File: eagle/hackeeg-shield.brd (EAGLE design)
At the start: 101.6 x 53.3 mm, 145 parts, among them IC1 ADS1299IPAG, IC10 TXB0108PWR, IC11 TXB0108PWR, IC2 TPS72325DBVT, IC3 TPS73225DBVT, IC5 24AA256UID, IC6 TPS60403DBVT, IC7 OPA376DBV, IC8 OPA376DBV, IC9 TXS0102DCUR

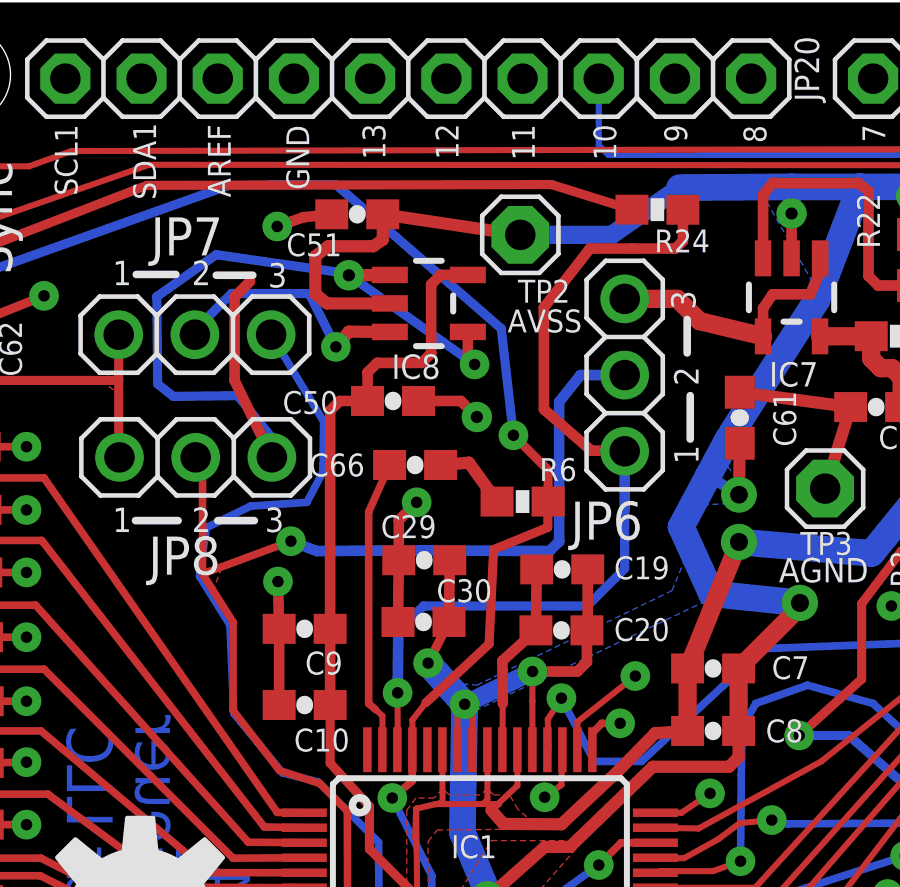
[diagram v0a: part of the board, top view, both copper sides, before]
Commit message: fixed problem with BIASOUT/BIASINV
- for common mode noise rejection
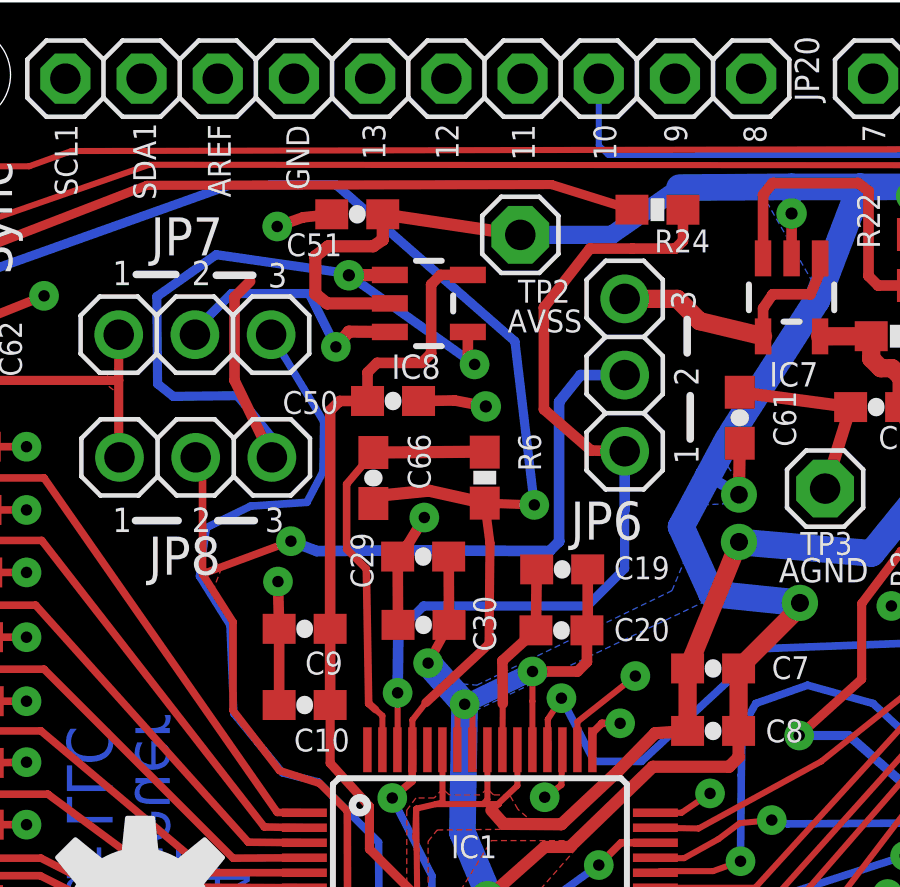
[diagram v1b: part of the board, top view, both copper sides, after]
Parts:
- moved R6 1.49 mm to (32.8, 37.5), turned to 90 degrees
- moved C66 1.46 mm to (29.1, 37.5), turned to 270 degrees
- moved C29 0.13 mm to (30.7, 34.9)
- moved C30 0.10 mm to (30.7, 32.6)
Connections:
- removed net N$22: C66.2, R6.1
- removed net N$25: C66.1, IC1.63
- new net BIASOUT: C66.1, IC1.63, R6.2
- net BIASINV: now also C66.2, R6.1; no longer R6.2
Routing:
- net BIASOUT: track 0.00 -> 14.4 mm
- net N$25: track 9.85 -> 0.00 mm
- net BIASINV: track 85.8 -> 89.9 mm
- net N$22: track 2.55 -> 0.00 mm
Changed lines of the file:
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@@
 <attribute name="VALUE" x="31.3436" y="21.3106" size="0.6096" layer="27"/>
 </element>
-<element name="C29" library="SparkFun-Passives" package="0603-CAP" value="1uF" x="30.7594" y="34.7472" smashed="yes">
-<attribute name="NAME" x="29.3116" y="35.4838" size="0.762" layer="25" font="vector" ratio="12"/>
-<attribute name="VALUE" x="29.7434" y="33.6042" size="0.4064" layer="27" font="vector"/>
-</element>
-<element name="C30" library="SparkFun-Passives" package="0603-CAP" value="1uF" x="30.734" y="32.6898" smashed="yes">
-<attribute name="NAME" x="31.1658" y="33.3502" size="0.762" layer="25" font="vector" ratio="12"/>
-<attribute name="VALUE" x="29.718" y="31.5468" size="0.4064" layer="27" font="vector"/>
+<element name="C29" library="SparkFun-Passives" package="0603-CAP" value="1uF" x="30.72256875" y="34.869375" smashed="yes">
+<attribute name="NAME" x="29.063946875" y="33.812734375" size="0.762" layer="25" font="vector" ratio="12" rot="R90"/>
+<attribute name="VALUE" x="29.70656875" y="33.726375" size="0.4064" layer="27" font="vector"/>
+</element>
+<element name="C30" library="SparkFun-Passives" package="0603-CAP" value="1uF" x="30.734" y="32.592009375" smashed="yes">
+<attribute name="NAME" x="33.151825" y="31.70529375" size="0.762" layer="25" font="vector" ratio="12" rot="R90"/>
+<attribute name="VALUE" x="29.718" y="31.449009375" size="0.4064" layer="27" font="vector"/>
 </element>
 <element name="C31" library="SparkFun-Passives" package="0603-CAP" value="0.01uF" x="82.677" y="47.244" smashed="yes">
@@
 <attribute name="VALUE" x="56.515" y="39.8272" size="0.4064" layer="27" font="vector" rot="R270"/>
 </element>
-<element name="C66" library="SparkFun-Passives" package="0603-CAP" value="0.01uF" x="30.4546" y="37.9222" smashed="yes">
-<attribute name="NAME" x="26.924" y="37.5412" size="0.762" layer="25" font="vector" ratio="12"/>
-<attribute name="VALUE" x="29.4386" y="36.7792" size="0.4064" layer="27" font="vector"/>
-</element>
-<element name="R6" library="SparkFun-Passives" package="0603-RES" value="3.98K" x="34.036" y="36.703" smashed="yes">
-<attribute name="NAME" x="34.5948" y="37.3888" size="0.762" layer="25" font="vector" ratio="12"/>
-<attribute name="VALUE" x="33.02" y="35.56" size="0.4064" layer="27" font="vector"/>
+<element name="C66" library="SparkFun-Passives" package="0603-CAP" value="0.01uF" x="29.062425" y="37.48760625" smashed="yes" rot="R270">
+<attribute name="NAME" x="30.210503125" y="38.961315625" size="0.762" layer="25" font="vector" ratio="12" rot="R270"/>
+<attribute name="VALUE" x="27.919425" y="38.50360625" size="0.4064" layer="27" font="vector" rot="R270"/>
+</element>
+<element name="R6" library="SparkFun-Passives" package="0603-RES" value="3.98K" x="32.774890625" y="37.500809375" smashed="yes" rot="R90">
+<attribute name="NAME" x="34.65220625" y="37.71798125" size="0.762" layer="25" font="vector" ratio="12" rot="R90"/>
+<attribute name="VALUE" x="33.917890625" y="36.484809375" size="0.4064" layer="27" font="vector" rot="R90"/>
 </element>
 <element name="C68" library="SparkFun-Passives" package="0603-CAP" value="1uF" x="51.2572" y="39.116" smashed="yes" rot="R180">
@@
 <wire x1="54.1884" y1="46.0629" x2="54.5567" y2="46.3042" width="0.4064" layer="1"/>
 <wire x1="54.5567" y1="46.3042" x2="56.0714" y2="46.3042" width="0.4064" layer="1"/>
-<wire x1="29.9094" y1="34.7472" x2="29.884" y2="32.6898" width="0.3556" layer="1"/>
+<wire x1="29.87256875" y1="34.869375" x2="29.884" y2="32.592009375" width="0.3556" layer="1"/>
 <wire x1="48.9998" y1="26.935" x2="49.265" y2="26.935" width="0.2032" layer="1"/>
 <wire x1="49.265" y1="26.935" x2="49.276" y2="26.924" width="0.2032" layer="1"/>
@@
 <via x="56.7182" y="33.6804" extent="1-16" drill="0.381"/>
 <wire x1="56.7182" y1="33.6804" x2="56.642" y2="33.4772" width="0.3556" layer="2"/>
-<wire x1="29.9094" y1="34.7472" x2="29.9094" y2="36.0816" width="0.3556" layer="1"/>
-<wire x1="29.9094" y1="36.0816" x2="30.5054" y2="36.6776" width="0.3556" layer="1"/>
-<via x="30.5054" y="36.6776" extent="1-16" drill="0.381"/>
+<wire x1="29.87256875" y1="34.869375" x2="30.20175" y2="35.254325" width="0.3556" layer="1"/>
+<wire x1="30.20175" y1="35.254325" x2="30.760671875" y2="36.171128125" width="0.3556" layer="1"/>
+<via x="30.760671875" y="36.171128125" extent="1-16" drill="0.381"/>
 <via x="56.3372" y="37.9476" extent="1-16" drill="0.6096"/>
 <wire x1="57.658" y1="37.9612" x2="57.6444" y2="37.9476" width="0.3556" layer="1"/>
@@
 <wire x1="44.9716" y1="39.8526" x2="41.275" y2="40.347" width="0.4064" layer="1"/>
 <wire x1="44.9716" y1="39.8526" x2="44.1198" y2="37.1348" width="0.4064" layer="1"/>
-<wire x1="30.568" y1="40.0558" x2="31.9786" y2="40.0558" width="0.3556" layer="1"/>
-<wire x1="31.9786" y1="40.0558" x2="32.512" y2="39.5224" width="0.3556" layer="1"/>
-<via x="32.512" y="39.5224" extent="1-16" drill="0.4064"/>
+<wire x1="30.568" y1="40.0558" x2="31.76778125" y2="40.073578125" width="0.3556" layer="1"/>
+<wire x1="31.76778125" y1="40.073578125" x2="32.810703125" y2="39.873934375" width="0.3556" layer="1"/>
+<via x="32.810703125" y="39.873934375" extent="1-16" drill="0.4064"/>
 </signal>
 <signal name="N$7">
@@
 <wire x1="89.4842" y1="42.3672" x2="87.796" y2="42.9768" width="0.6096" layer="1"/>
 <wire x1="87.796" y1="42.9768" x2="86.0552" y2="42.9886" width="0.6096" layer="1"/>
-<wire x1="31.6094" y1="34.7472" x2="31.584" y2="32.6898" width="0.3556" layer="1"/>
+<wire x1="31.57256875" y1="34.869375" x2="31.584" y2="32.592009375" width="0.3556" layer="1"/>
 <wire x1="36.322" y1="16.764" x2="36.3636" y2="16.7306" width="0.1524" layer="1"/>
 <wire x1="31.8516" y1="16.764" x2="31.8636" y2="16.7306" width="0.1524" layer="1"/>
@@
 <wire x1="29.5656" y1="14.1732" x2="28.9306" y2="14.1732" width="0.3048" layer="1"/>
 <wire x1="26.5294" y1="14.1732" x2="26.5294" y2="11.7602" width="0.4064" layer="1"/>
-<wire x1="31.584" y1="32.6898" x2="30.8864" y2="31.3182" width="0.3048" layer="1"/>
+<wire x1="31.584" y1="32.592009375" x2="30.8864" y2="31.3182" width="0.3048" layer="1"/>
 <via x="30.8864" y="31.3182" extent="1-16" drill="0.381"/>
 <wire x1="30.8864" y1="31.3182" x2="32.1056" y2="29.9466" width="0.889" layer="16"/>
@@
 <signal name="BIASINV">
 <contactref element="IC1" pad="61"/>
-<contactref element="R6" pad="2"/>
-<wire x1="34.886" y1="36.703" x2="34.8742" y2="35.8394" width="0.3048" layer="1"/>
-<wire x1="34.8742" y1="35.8394" x2="33.0708" y2="35.1028" width="0.3048" layer="1"/>
-<wire x1="33.0708" y1="35.1028" x2="32.9184" y2="31.9532" width="0.3048" layer="1"/>
+<wire x1="32.948628125" y1="35.3164125" x2="32.9184" y2="31.9532" width="0.3048" layer="1"/>
 <wire x1="32.9184" y1="31.9532" x2="30.8102" y2="29.9974" width="0.3048" layer="1"/>
 <wire x1="30.8102" y1="29.9974" x2="30.3636" y2="29.4238" width="0.2032" layer="1"/>
@@
 <contactref element="JP15" pad="1"/>
 <wire x1="24.257" y1="47.244" x2="27.813" y2="47.2694" width="0.3048" layer="16"/>
-<wire x1="27.813" y1="47.2694" x2="33.3248" y2="42.4688" width="0.3048" layer="16"/>
-<wire x1="34.886" y1="36.703" x2="34.886" y2="37.758" width="0.3048" layer="1"/>
-<wire x1="34.886" y1="37.758" x2="33.7312" y2="38.9128" width="0.3048" layer="1"/>
-<via x="33.7312" y="38.9128" extent="1-16" drill="0.381"/>
-<wire x1="33.7312" y1="38.9128" x2="33.3248" y2="42.4688" width="0.3048" layer="16"/>
+<wire x1="27.813" y1="47.2694" x2="33.780475" y2="42.04335" width="0.3048" layer="16"/>
+<via x="34.42715625" y="36.591746875" extent="1-16" drill="0.381"/>
+<wire x1="34.42715625" y1="36.591746875" x2="33.780475" y2="42.04335" width="0.3048" layer="16"/>
 <contactref element="JP16" pad="3"/>
 <wire x1="14.859" y1="43.8912" x2="9.8806" y2="43.7896" width="0.3048" layer="16"/>
@@
 <wire x1="6.8326" y1="8.1788" x2="9.8552" y2="5.6642" width="0.254" layer="16"/>
 <wire x1="24.257" y1="47.244" x2="14.859" y2="43.8912" width="0.3048" layer="16"/>
-</signal>
-<signal name="N$22">
-<contactref element="R6" pad="1"/>
 <contactref element="C66" pad="2"/>
-<wire x1="31.3046" y1="37.9222" x2="32.2462" y2="38.0002" width="0.4064" layer="1"/>
-<wire x1="32.2462" y1="38.0002" x2="33.186" y2="36.703" width="0.4064" layer="1"/>
+<contactref element="R6" pad="1"/>
+<wire x1="29.062425" y1="36.63760625" x2="29.388678125" y2="36.913059375" width="0.4064" layer="1"/>
+<wire x1="29.388678125" y1="36.913059375" x2="30.912309375" y2="37.065459375" width="0.4064" layer="1"/>
+<wire x1="30.912309375" y1="37.065459375" x2="32.774890625" y2="36.650809375" width="0.4064" layer="1"/>
+<wire x1="32.948628125" y1="35.3164125" x2="32.774890625" y2="36.650809375" width="0.3048" layer="1"/>
+<wire x1="32.774890625" y1="36.650809375" x2="34.42715625" y2="36.591746875" width="0.3048" layer="1"/>
 </signal>
-<signal name="N$25">
+<signal name="BIASOUT">
 <contactref element="C66" pad="1"/>
 <contactref element="IC1" pad="63"/>
-<wire x1="29.6046" y1="37.9222" x2="28.9052" y2="36.3592" width="0.254" layer="1"/>
-<wire x1="28.9052" y1="36.3592" x2="28.9052" y2="29.972" width="0.254" layer="1"/>
+<wire x1="29.062425" y1="38.33760625" x2="28.17063125" y2="37.284521875" width="0.254" layer="1"/>
+<wire x1="28.17063125" y1="37.284521875" x2="28.17063125" y2="35.117025" width="0.254" layer="1"/>
+<wire x1="28.17063125" y1="35.117025" x2="28.8282375" y2="34.45941875" width="0.254" layer="1"/>
+<wire x1="28.8282375" y1="34.45941875" x2="28.9052" y2="29.972" width="0.254" layer="1"/>
 <wire x1="28.9052" y1="29.972" x2="29.1338" y2="29.7688" width="0.254" layer="1"/>
 <wire x1="29.1338" y1="29.7688" x2="29.3636" y2="29.5644" width="0.2032" layer="1"/>
 <wire x1="29.3636" y1="29.5644" x2="29.3636" y2="28.4306" width="0.2032" layer="1"/>
+<contactref element="R6" pad="2"/>
+<wire x1="29.062425" y1="38.33760625" x2="32.495490625" y2="38.36300625" width="0.4064" layer="1"/>
+<wire x1="32.495490625" y1="38.36300625" x2="32.774890625" y2="38.350809375" width="0.4064" layer="1"/>
 </signal>
 <signal name="VCC_5V_FILTERED">

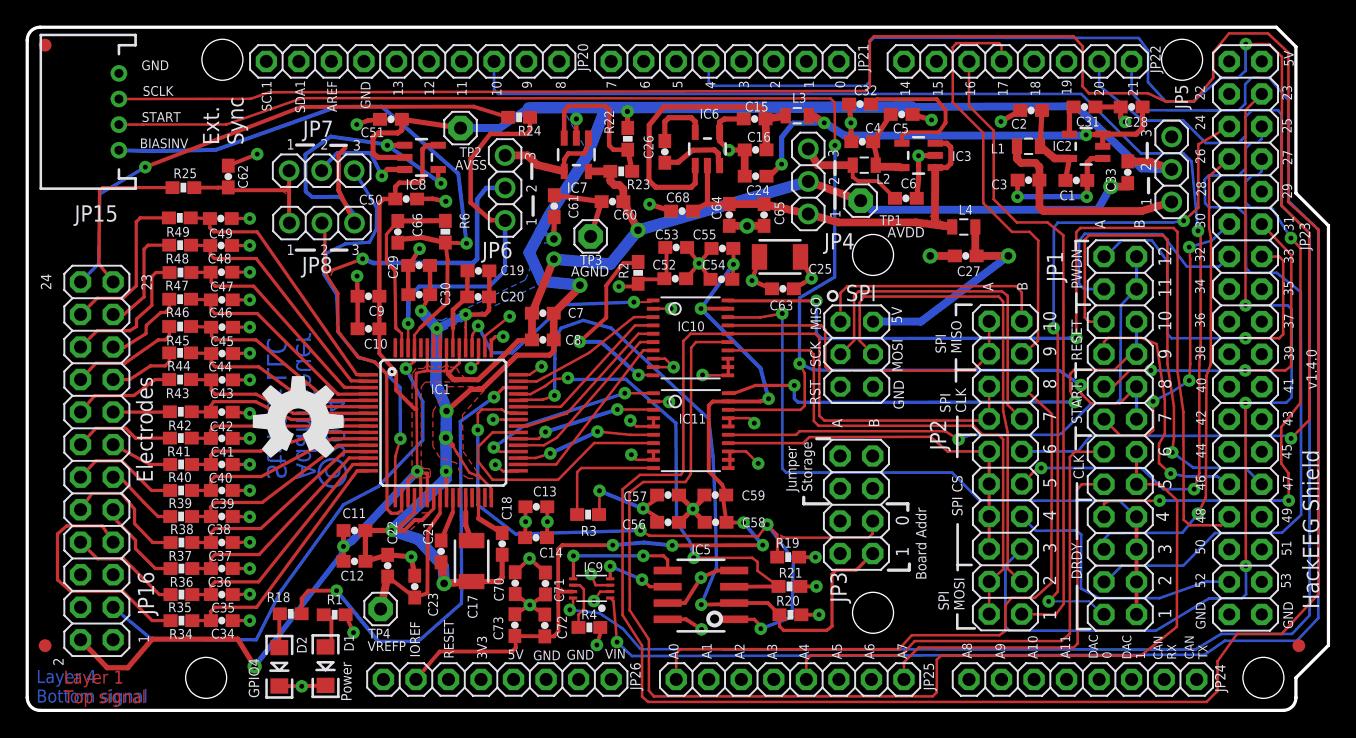
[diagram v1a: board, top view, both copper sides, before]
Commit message: added JP9 - BIASIN/BIAS_ELEC/BIASOUT config
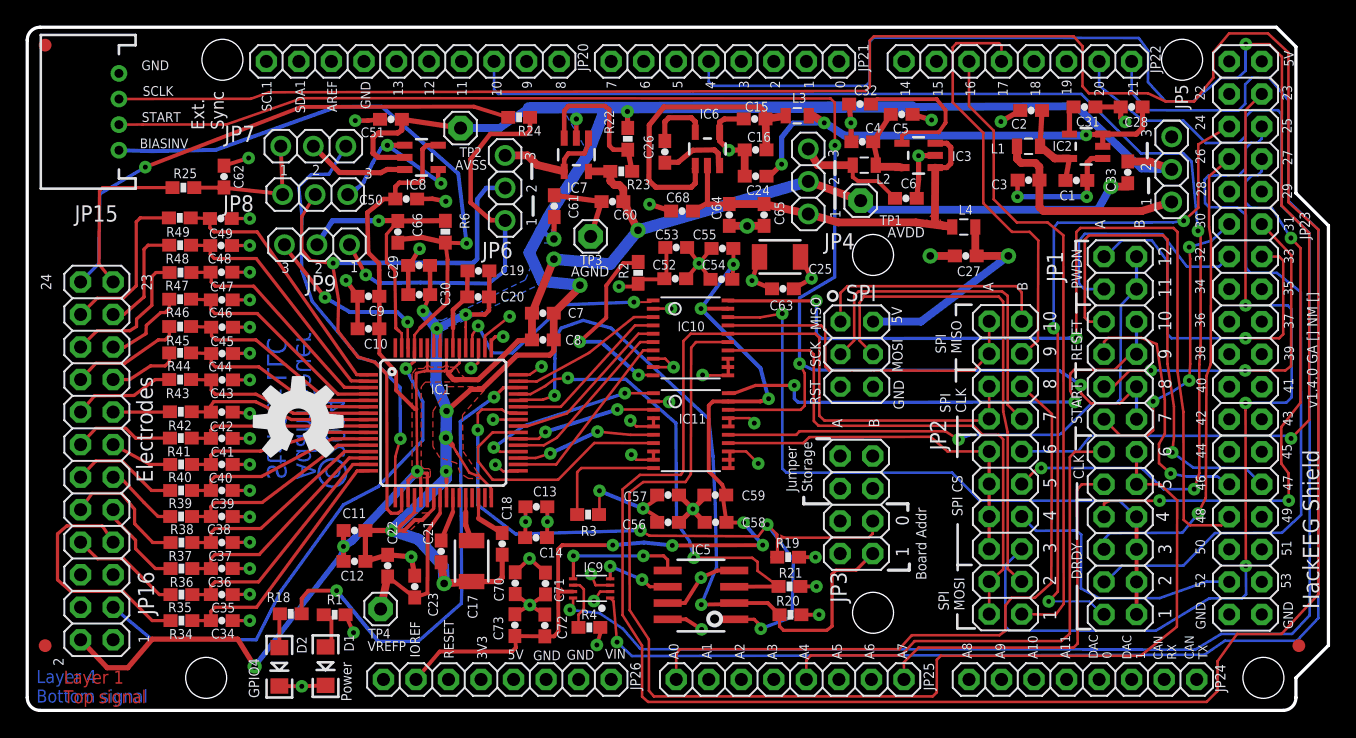
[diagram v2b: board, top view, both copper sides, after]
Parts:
- added JP9: BIASOUT_BIASIN_BIAS_ELEC, headers:1X03
- moved JP8 2.29 mm to (22.6, 40.4)
- moved JP7 2.02 mm to (22.5, 44.2)
- moved C62 0.33 mm to (15.5, 41.8)
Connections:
- new net BIASIN: IC1.62, JP9.3
- net BIASOUT: now also JP9.2
- net BIAS_ELEC: now also JP9.1; no longer IC1.62
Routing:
- net N$17: track 29.2 -> 13.1 mm
- net BIASIN: track 0.00 -> 14.3 mm, vias 0 -> 2
- net BIASOUT: track 14.4 -> 22.1 mm, vias 0 -> 1
- net SRB1: track 46.5 -> 49.6 mm
- net BIAS_ELEC: track 30.3 -> 32.0 mm
- net SRB2: track 31.5 -> 32.9 mm
- net AVDD: track 160.3 -> 161.1 mm
- net REF_ELEC: track 11.6 -> 10.8 mm
- net N$16: track 8.49 -> 8.07 mm, vias 1 -> 0
- removed copper zone on layer 1, net REF_ELEC
- removed copper zone on layer 1, net SRB1
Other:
- board text added: "v1.4.0 GA [] NM []"
- board text removed: "v1.4.0"

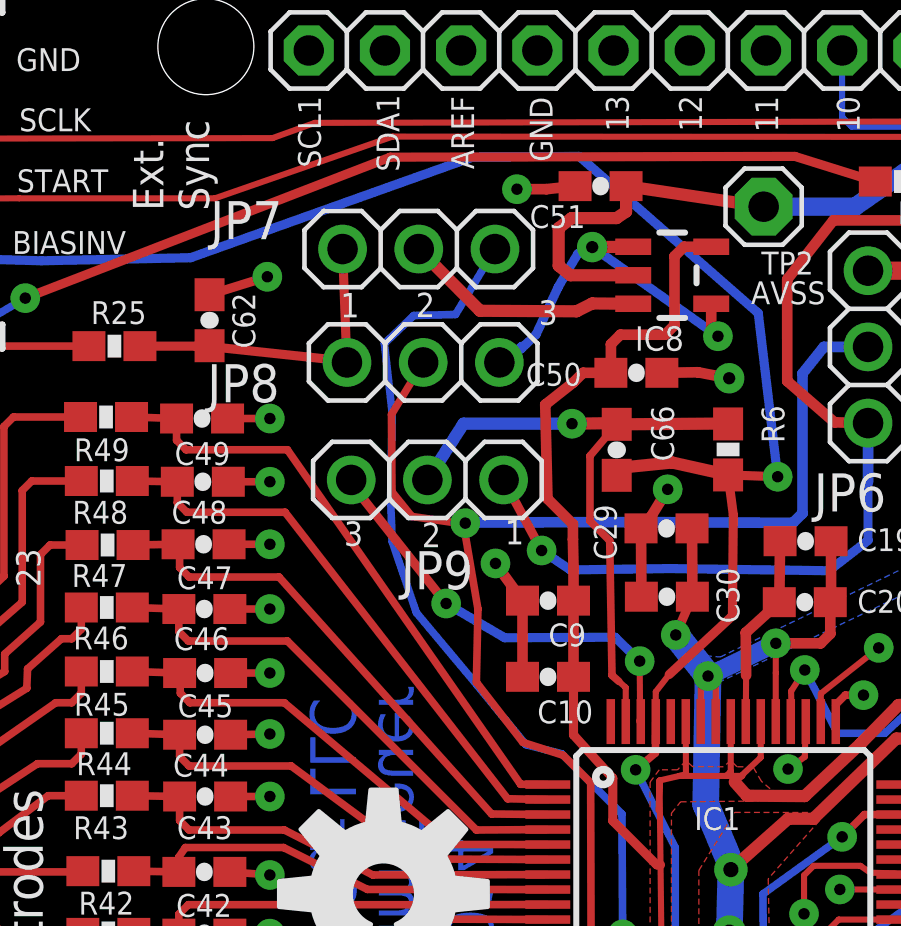
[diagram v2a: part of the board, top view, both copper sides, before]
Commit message: minor routing adjustments
- for JP9 clearance
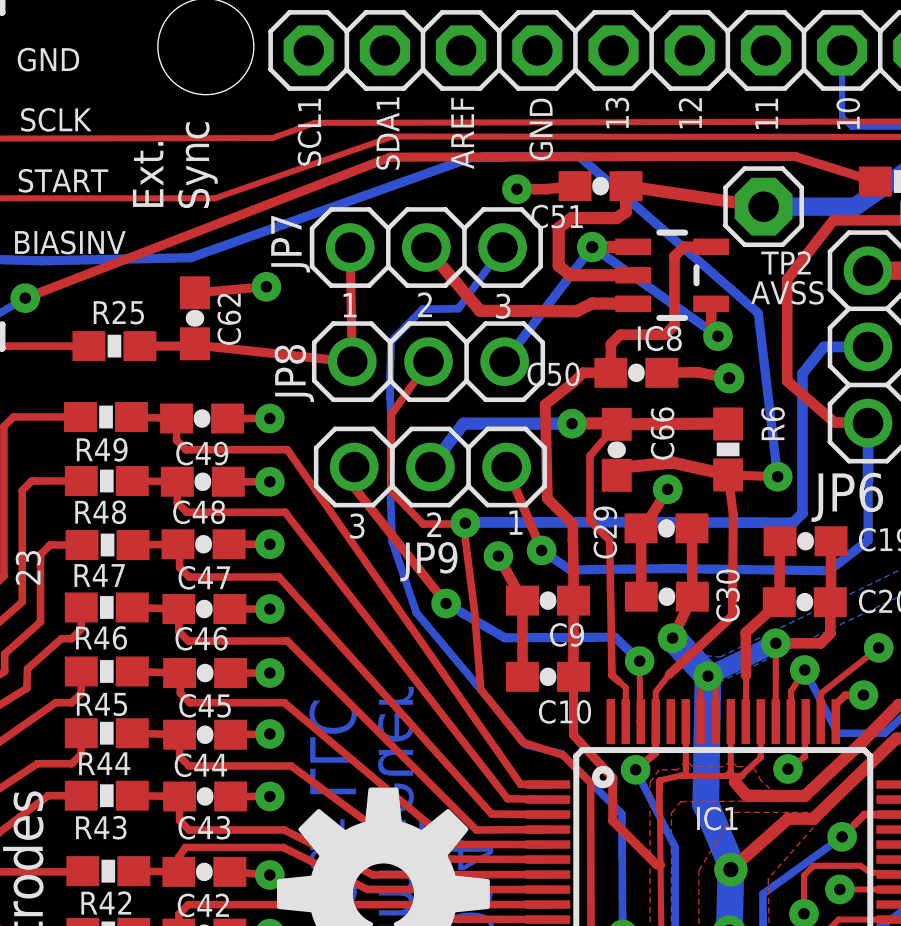
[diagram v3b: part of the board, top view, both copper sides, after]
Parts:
- moved C62 0.49 mm to (15.0, 41.9)
- moved JP9 0.44 mm to (22.9, 36.9)
- moved JP7 0.26 mm to (22.7, 44.2)
- moved JP8 0.18 mm to (22.8, 40.4)
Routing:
- net AGND: track 148.9 -> 149.4 mm
- net N$17: track 13.1 -> 12.6 mm
